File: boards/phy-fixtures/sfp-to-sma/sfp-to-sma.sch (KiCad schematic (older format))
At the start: 37 parts, among them J1 SFP_CAGE, J10 901-10511-3, J11 901-10511-3, J2 CONN_3_PWROUT, J3 Conn_01x03, J4 Conn_01x03, J5 CONN_SFP_HOST, J6 Conn_01x02, J7 Conn_01x03, J8 901-10511-3, J9 901-10511-3

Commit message: Final schematic for sfp-to-sma test fixture
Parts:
- removed J7: Conn_01x03, symbol Connector:Conn_01x03
- added C10, C9: 0.47 uF, symbol device:C
- added C7, C8: 4.7 uF, symbol device:C
- added D4, D5: RED, symbol device:LED
- added D6: GREEN, symbol device:LED
- added FB3, FB4: 600R, symbol passive-azonenberg:INDUCTOR_PWROUT
- added J12, J13, J14, J15, J16, J17, J18, J19, J20, J21, J23, J24, J25, J26, J27: Conn_01x02, symbol Connector:Conn_01x02
- added J22: CONN_SFP_HOST, symbol special-azonenberg:CONN_SFP_HOST
- added J28: Conn_01x05, symbol Connector:Conn_01x05
- added J7: SFP_CAGE, symbol Connector:Conn_01x01
- added Q1, Q2: SSM6N58NU, symbol special-azonenberg:SSM6N58NU_DUAL_NMOS
- added R11, R16: 1K, symbol device:R
- added R12, R13, R14, R15: 4.7K, symbol device:R
- added R17, R18, R19, R20: PS1608GT2-R50-T1, symbol analog-azonenberg:SPLITTER_SUSUMU_PS
- added R21, R22, R23, R24: 470, symbol device:R
- R2: value 470 -> 4.7K
- R8: value 10K -> 4.7K
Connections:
- net 3V3: now also D2.2 (A), D3.2 (A), R2.1, R8.1, D4.2 (A), D5.2 (A), FB3.2, FB4.2, J27.2 (Pin_2), R12.1, R13.1, R14.1, R15.1, R24.1
- net GND: now also C10.2, C7.2, C8.2, C9.2, J22.1 (GND_TX), J22.10 (GND_RX), J22.11 (GND_RX), J22.14 (GND_RX), J22.17 (GND_TX), J22.20 (GND_TX), J28.5 (Pin_5), J7.1 (Pin_1), Q1.S1 (S), Q1.S2 (S), Q2.S1 (S), Q2.S2 (S), R17.4 (GND), R18.4 (GND), R19.4 (GND), R20.4 (GND); no longer D2.1 (K), D3.1 (K), R8.1
- net RS0: now also J22.7 (RS0)
- net RS1: now also J22.9 (RS1)
- net at R1.1: now also D2.1 (K); no longer D2.2 (A)
- net I2C_SCL: no longer names the net of R9.2
- net I2C_SCL: now also J20.2 (Pin_2); no longer J5.5 (SCL)
- net I2C_SDA: no longer names the net of R10.2
- net I2C_SDA: now also J21.2 (Pin_2); no longer J5.4 (SDA)
- net MOD_ABS renamed MOD_ABS1
- net MOD_ABS1: now also J13.1 (Pin_1)
- net RX_LOS: no longer names the net of R1.2
- net RX_LOS: now also Q1.D1 (D); no longer J5.8 (RX_LOS)
- net RX_N renamed RX1_N
- net RX1_N: now also R18.1 (IN); no longer J9.1 (In)
- net RX_P renamed RX1_P
- net RX1_P: now also R17.1 (IN); no longer J8.1 (In)
- removed net TX_DISABLE: J5.3 (TX_DISABLE), J6.1 (Pin_1), R8.2
- net TX_FAULT: no longer names the net of R2.2
- net TX_FAULT: now also J18.2 (Pin_2); no longer J5.2 (TX_FAULT)
- net TX_N renamed TX1_N
- net TX1_N: now also R20.2 (OUT0); no longer J11.1 (In)
- net TX_P renamed TX1_P
- net TX1_P: now also R19.2 (OUT0); no longer J10.1 (In)
- net VDD_RX renamed VDD_RX1
- net VDD_TX renamed VDD_TX1
- new net: J6.1 (Pin_1), R11.2
- new net: J25.2 (Pin_2), R14.2
- new net: J26.2 (Pin_2), R15.2
- new net: J27.1 (Pin_1), R16.2
- new net: D6.2 (A), R24.2
- new net: J23.2 (Pin_2), R12.2
- new net: J24.2 (Pin_2), R13.2
- new net: D3.1 (K), R21.1
- new net: Q1.D2 (D), R21.2
- new net: J19.2 (Pin_2), R8.2
- new net: D4.1 (K), R22.1
- new net: Q2.D1 (D), R22.2
- new net: D5.1 (K), R23.1
- new net: Q2.D2 (D), R23.2
- new net I2C_SCL1: J14.1 (Pin_1), J20.1 (Pin_1), J28.1 (Pin_1), J5.5 (SCL)
- new net I2C_SCL2: J14.2 (Pin_2), J22.5 (SCL), J25.1 (Pin_1), J28.3 (Pin_3)
- new net I2C_SDA1: J17.1 (Pin_1), J21.1 (Pin_1), J28.2 (Pin_2), J5.4 (SDA)
- new net I2C_SDA2: J17.2 (Pin_2), J22.4 (SDA), J26.1 (Pin_1), J28.4 (Pin_4)
- new net MOD_ABS2: D6.1 (K), J13.2 (Pin_2), J22.6 (MOD_ABS)
- new net RX2_N: J22.12 (RX_N), R20.1 (IN)
- new net RX2_P: J22.13 (RX_P), R19.1 (IN)
- new net RX_LOS1: J12.1 (Pin_1), J23.1 (Pin_1), J5.8 (RX_LOS), Q1.G1 (G)
- new net RX_LOS2: J12.2 (Pin_2), J22.8 (RX_LOS), J24.1 (Pin_1), Q1.G2 (G)
- new net RX_TAP_N: J9.1 (In), R18.3 (OUT1)
- new net RX_TAP_P: J8.1 (In), R17.3 (OUT1)
- new net TX2_N: J22.19 (TX_N), R18.2 (OUT0)
- new net TX2_P: J22.18 (TX_P), R17.2 (OUT0)
- new net TX_DISABLE1: J15.1 (Pin_1), J5.3 (TX_DISABLE), R11.1
- new net TX_DISABLE2: J15.2 (Pin_2), J22.3 (TX_DISABLE), R16.1
- new net TX_FAULT1: J16.1 (Pin_1), J18.1 (Pin_1), J5.2 (TX_FAULT), Q2.G1 (G)
- new net TX_FAULT2: J16.2 (Pin_2), J19.1 (Pin_1), J22.2 (TX_FAULT), Q2.G2 (G)
- new net TX_TAP_N: J11.1 (In), R20.3 (OUT1)
- new net TX_TAP_P: J10.1 (In), R19.3 (OUT1)
- new net VDD_RX2: C10.1, C8.1, FB4.1, J22.15 (VDD_RX)
- new net VDD_TX2: C7.1, C9.1, FB3.1, J22.16 (VDD_TX)
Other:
- note added: "Control passthrough"
- note added: "Fault LEDs"
- note added: "Fault pullup enable"
- note added: "I2C pullup enable"
- note added: "LOS pullup enable"
- note added: "Loss-of-signal LEDs"
- note added: "Module 1 power filtering"
- note added: "Module 2 power filtering"
- note added: "Module-present LEDs"
- note added: "Rate select config"
- note added: "SMA splitters"
- note added: "TX disable"
- moved on the sheet: C3, C4, C5, C6, D1, D2, FB1, FB2, J10, J11, J3, J4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

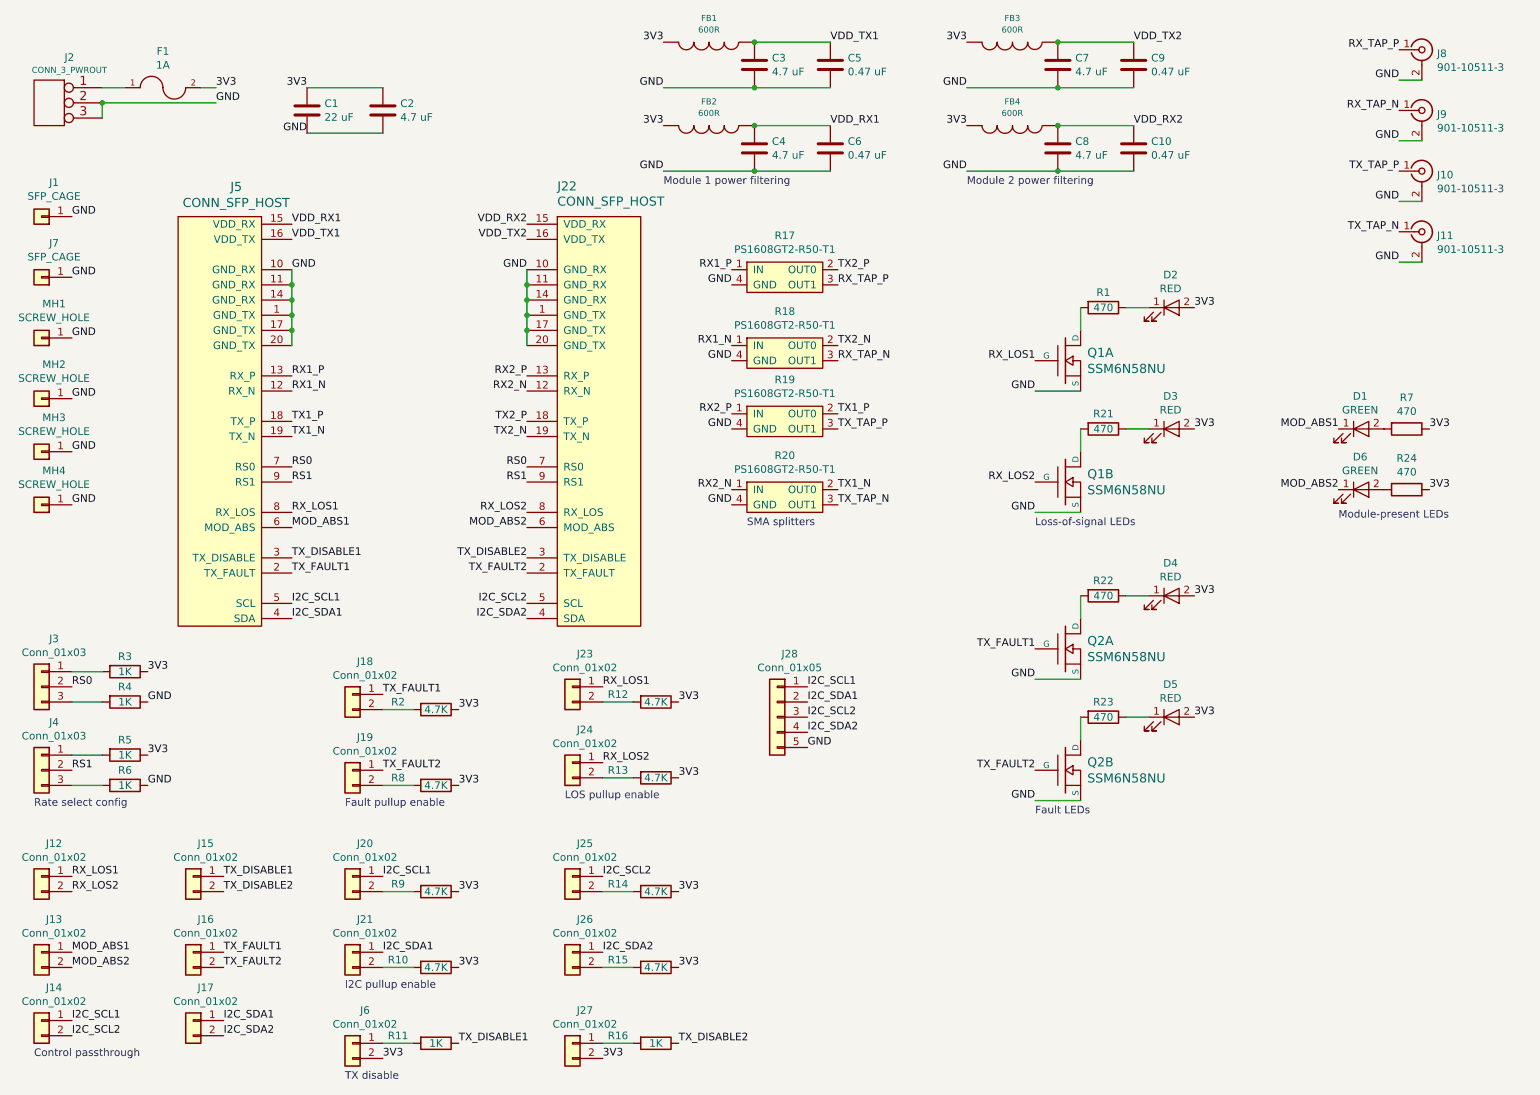
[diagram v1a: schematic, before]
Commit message: Routed most of sfp-to-sma
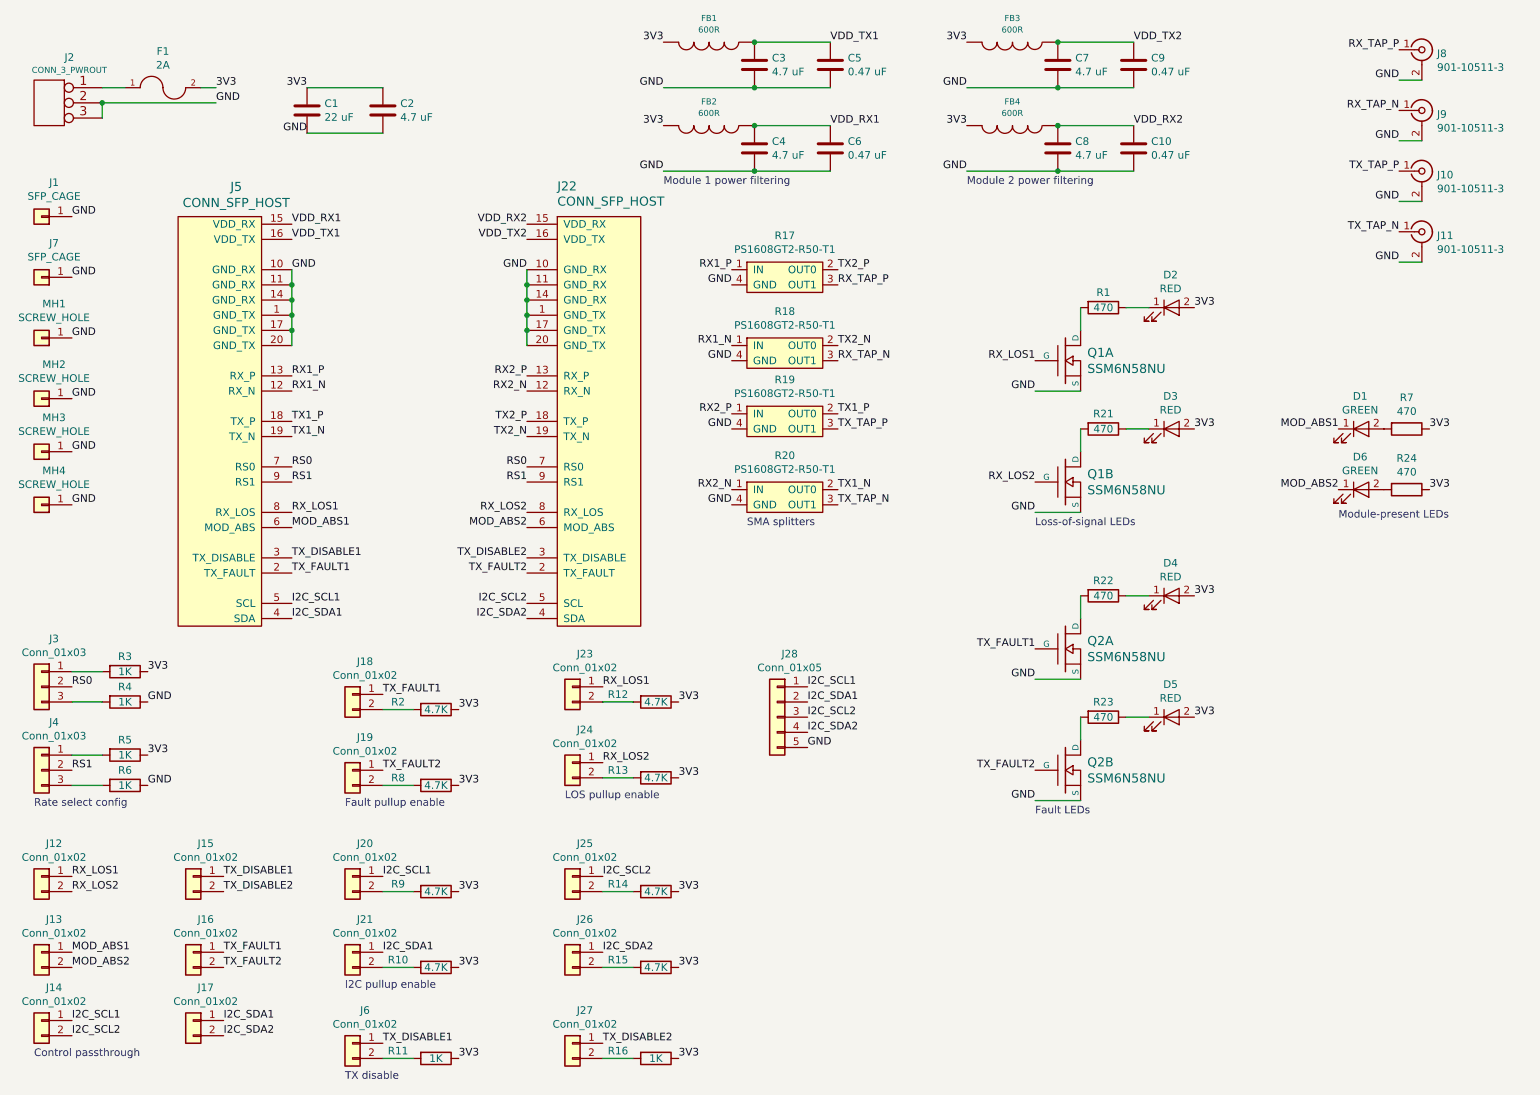
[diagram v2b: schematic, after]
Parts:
- C1: footprint (none) -> azonenberg_pcb:EIA_0805_CAP_NOSILK
- C10, C5, C6, C9: footprint (none) -> azonenberg_pcb:EIA_0402_CAP_NOSILK
- C2, C3, C4, C7, C8: footprint (none) -> azonenberg_pcb:EIA_0603_CAP_NOSILK
- D1, D2, D3, D4, D5, D6: footprint (none) -> azonenberg_pcb:EIA_0603_LED
- F1: value 1A -> 2A; footprint (none) -> azonenberg_pcb:EIA_0603_RES_NOSILK
- FB1, FB2, FB3, FB4: footprint (none) -> azonenberg_pcb:EIA_0603_INDUCTOR_NOSILK
- J1, J7: footprint (none) -> azonenberg_pcb:CONN_SFP_CAGE_TE_2007194-1
- J10, J11, J8, J9: footprint (none) -> azonenberg_pcb:CONN_SMA_EDGE_AMPHENOL_901_10511_3
- J12, J13, J14, J15, J16, J17, J18, J19, J20, J21, J23, J24, J25, J26, J27, J6: footprint (none) -> azonenberg_pcb:CONN_HEADER_2.54MM_1x2
- J2: footprint (none) -> azonenberg_pcb:CONN_CUI_PJ-058BH_HIPWR_BARREL_NOSLOT
- J22, J5: footprint (none) -> azonenberg_pcb:CONN_SFP+_AMPHENOL_UE76_A10_2000T
- J28: footprint (none) -> azonenberg_pcb:CONN_HEADER_2.54MM_1x5
- J3, J4: footprint (none) -> azonenberg_pcb:CONN_HEADER_2.54MM_1x3
- MH1, MH2, MH3, MH4: footprint (none) -> azonenberg_pcb:MECHANICAL_CLEARANCEHOLE_4_40
- Q1, Q2: footprint (none) -> azonenberg_pcb:DFN_6_0.65MM_2x2MM_GDS
- R1, R10, R11, R12, R13, R14, R15, R16, R2, R21, R22, R23, R24, R3, R4, R5, R6, R7, R8, R9: footprint (none) -> azonenberg_pcb:EIA_0402_RES_NOSILK
- R17, R18, R19, R20: footprint (none) -> azonenberg_pcb:SPLITTER_SUSUMU_PS1608G
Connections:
- net 3V3: now also R11.1, R16.1; no longer J27.2 (Pin_2), J6.2 (Pin_2)
- net TX_DISABLE1: now also J6.1 (Pin_1); no longer R11.1
- net TX_DISABLE2: now also J27.1 (Pin_1); no longer R16.1
- net at R11.2: now also J6.2 (Pin_2); no longer J6.1 (Pin_1)
- net at R16.2: now also J27.2 (Pin_2); no longer J27.1 (Pin_1)
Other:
- moved on the sheet: R11, R16

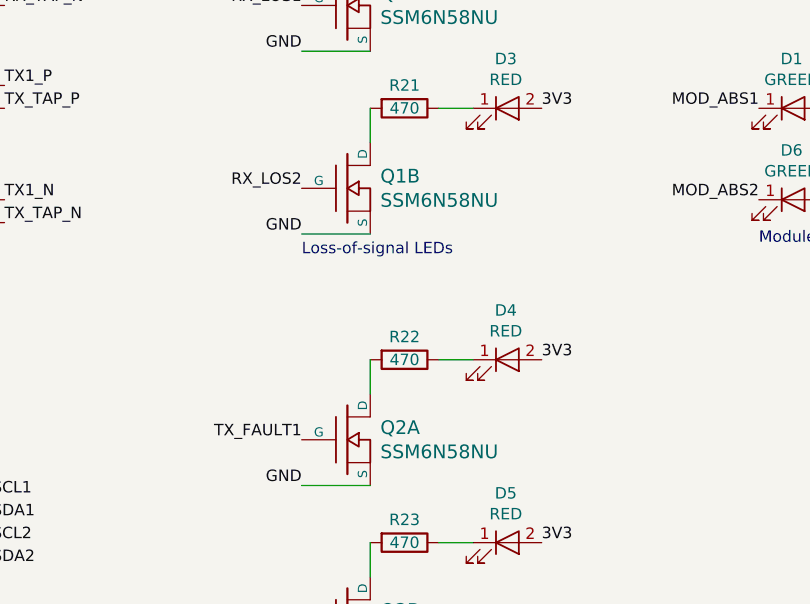
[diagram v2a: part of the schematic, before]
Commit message: Continued layout on sfp-to-sma board. Fully routed, need some plane tweaks and stitching vias.
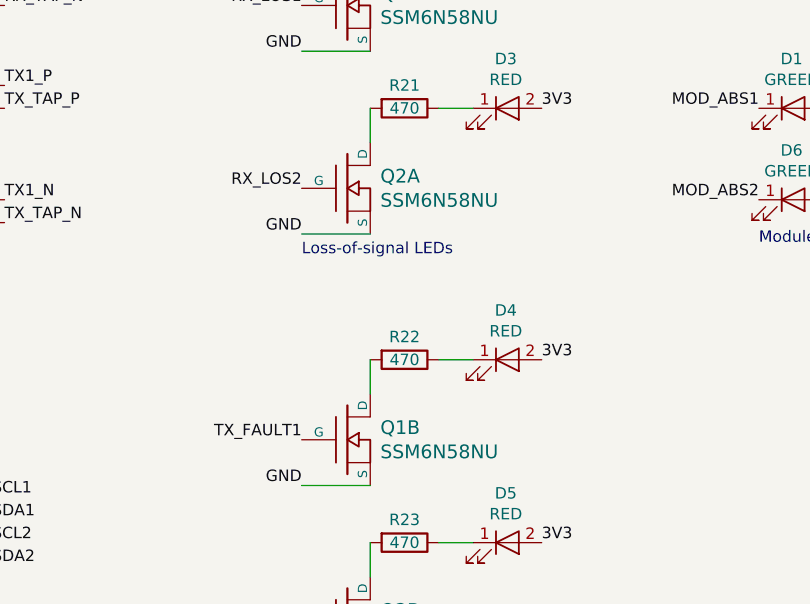
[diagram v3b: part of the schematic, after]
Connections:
- net RX_LOS2: now also Q2.G1 (G); no longer Q1.G2 (G)
- net TX_FAULT1: now also Q1.G2 (G); no longer Q2.G1 (G)
- net at R21.2: now also Q2.D1 (D); no longer Q1.D2 (D)
- net at R22.2: now also Q1.D2 (D); no longer Q2.D1 (D)
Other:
- moved on the sheet: Q1B, Q2A
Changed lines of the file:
@@
 	0    1    1    0
-$EndComp
-$Comp
-L special-azonenberg:SSM6N58NU_DUAL_NMOS Q1
-U 2 1 5EEC463F
-P 7700 3600
-F 0 "Q1" H 7844 3653 60  0000 L CNN
-F 1 "SSM6N58NU" H 7844 3547 60  0000 L CNN
-F 2 "azonenberg_pcb:DFN_6_0.65MM_2x2MM_GDS" H 7700 3600 60  0001 C CNN
-F 3 "transistors/mos/*.*" H 7844 3494 60  0001 L CNN
-	2    7700 3600
-	1    0    0    -1
 $EndComp
 Text Label 7500 3600 2    50   ~ 0
@@
 	0    1    1    0
 $EndComp
-$Comp
-L special-azonenberg:SSM6N58NU_DUAL_NMOS Q2
-U 1 1 5EED1FE6
-P 7700 4700
-F 0 "Q2" H 7844 4753 60  0000 L CNN
-F 1 "SSM6N58NU" H 7844 4647 60  0000 L CNN
-F 2 "azonenberg_pcb:DFN_6_0.65MM_2x2MM_GDS" H 7700 4700 60  0001 C CNN
-F 3 "transistors/mos/*.*" H 7844 4594 60  0001 L CNN
-	1    7700 4700
-	1    0    0    -1
-$EndComp
 Text Label 7500 4900 2    50   ~ 0
 GND
@@
 Text Label 6000 5350 0    50   ~ 0
 GND
+$Comp
+L special-azonenberg:SSM6N58NU_DUAL_NMOS Q2
+U 1 1 5EED1FE6
+P 7700 3600
+F 0 "Q2" H 7844 3653 60  0000 L CNN
+F 1 "SSM6N58NU" H 7844 3547 60  0000 L CNN
+F 2 "azonenberg_pcb:DFN_6_0.65MM_2x2MM_GDS" H 7700 3600 60  0001 C CNN
+F 3 "transistors/mos/*.*" H 7844 3494 60  0001 L CNN
+	1    7700 3600
+	1    0    0    -1
+$EndComp
+$Comp
+L special-azonenberg:SSM6N58NU_DUAL_NMOS Q1
+U 2 1 5EEC463F
+P 7700 4700
+F 0 "Q1" H 7844 4753 60  0000 L CNN
+F 1 "SSM6N58NU" H 7844 4647 60  0000 L CNN
+F 2 "azonenberg_pcb:DFN_6_0.65MM_2x2MM_GDS" H 7700 4700 60  0001 C CNN
+F 3 "transistors/mos/*.*" H 7844 4594 60  0001 L CNN
+	2    7700 4700
+	1    0    0    -1
+$EndComp
 $EndSCHEMATC
